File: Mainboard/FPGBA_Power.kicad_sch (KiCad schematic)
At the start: 21 parts, among them U1 LM3880, U3 TPS22917DBV, U4 TLV62569DBV, U5 TLV75533PDBV, U6 TLV75518PDBV

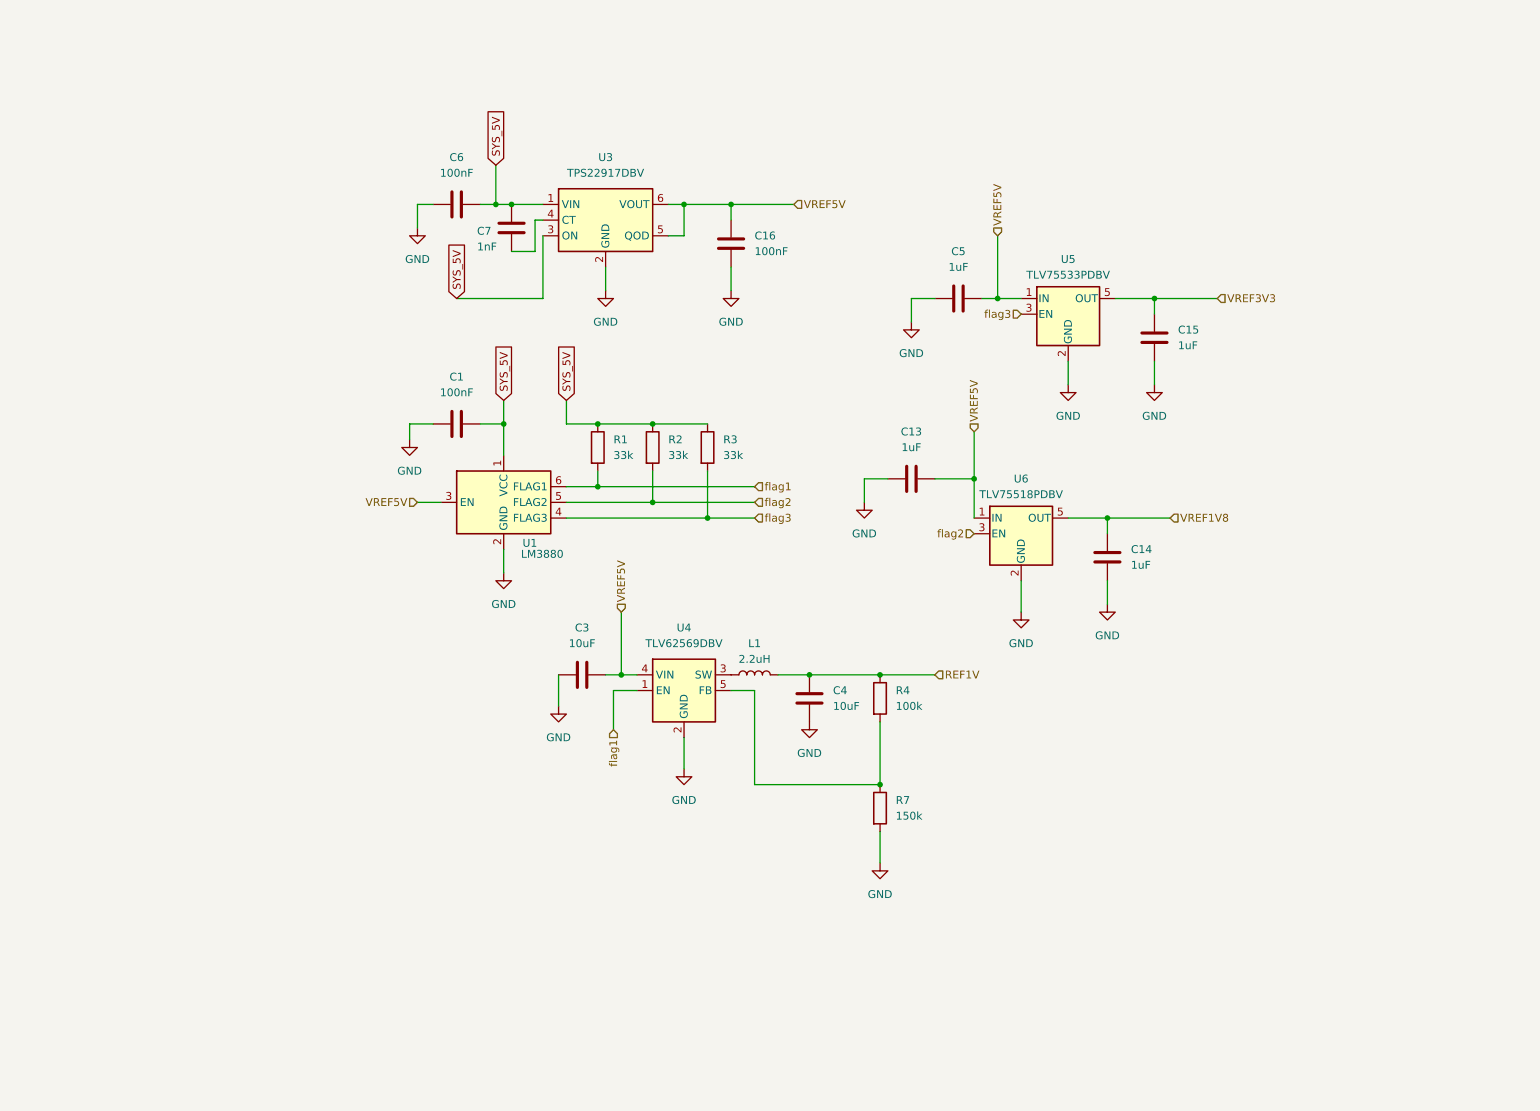
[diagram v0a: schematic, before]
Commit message: fixed heirarchy and dir structure
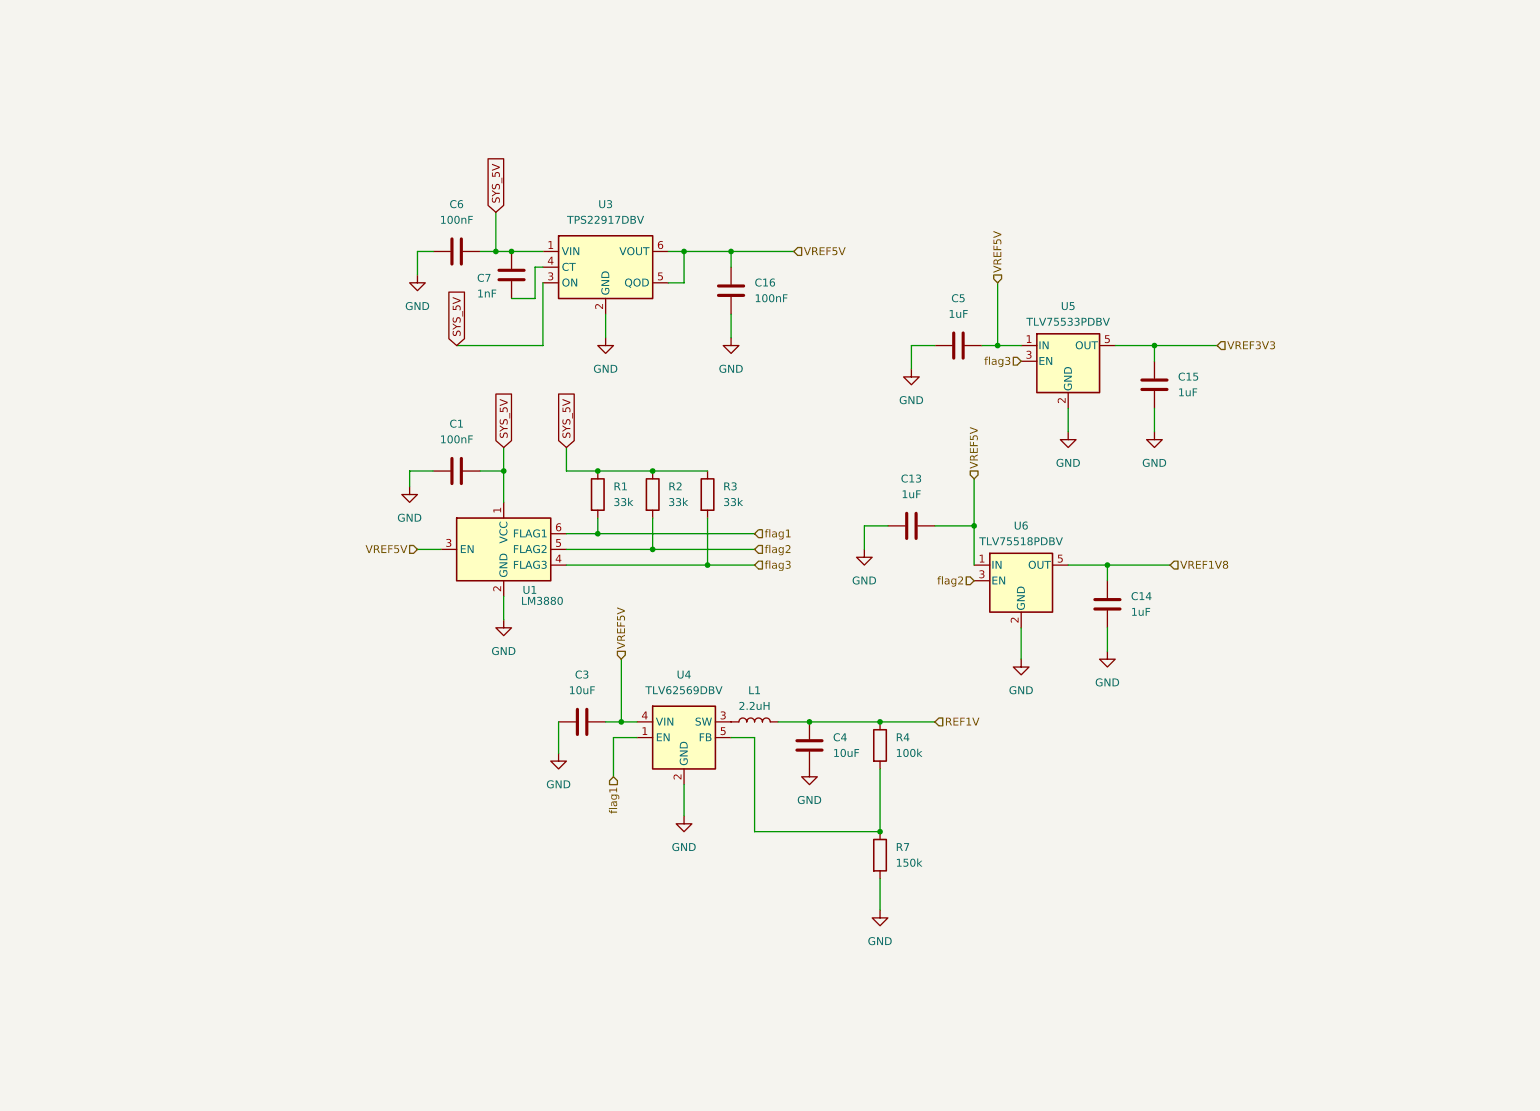
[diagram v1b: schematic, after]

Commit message: huge update: power/charging, audio, zif connections, screen, cartridge pinout
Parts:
- removed C15, C5: 1uF, Resistor_SMD:R_0603_1608Metric, symbol Device:C
- removed U5: TLV75533PDBV, Package_TO_SOT_SMD:SOT-23-5, symbol Regulator_Linear:TLV75533PDBV
- added C17: 10uF, Capacitor_SMD:C_0603_1608Metric, symbol Device:C
- added C18: 22uF, Capacitor_SMD:C_0603_1608Metric, symbol Device:C
- added IC3: XC7S50-L1CSGA324I, Package_BGA:BGA-324_15x15mm_Layout18x18_P0.8mm, symbol XC7S50-L1CSGA324I:XC7S50-L1CSGA324I
- added L3: 2.2uH, FPGBA:1206 (metric 2832), symbol Device:L
- added R10: 100k, Resistor_SMD:R_0603_1608Metric, symbol Device:R
- added R9: 453k, Resistor_SMD:R_0603_1608Metric, symbol Device:R
- added U7: TPS62822DLC, Package_SON:Texas_VSON-HR-8_1.5x2mm_P0.5mm, symbol Regulator_Switching:TPS62822DLC
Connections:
- net GND: now also C17.1, C18.1, IC3.A1 (GND_1), IC3.A12 (GND_2), IC3.A18 (GND_3), IC3.B9 (GND_4), IC3.C16 (GND_6), IC3.C6 (GND_5), IC3.D13 (GND_8), IC3.D3 (GND_7), IC3.E10 (GND_10), IC3.E8 (GND_9), IC3.F11 (GND_13), IC3.F17 (GND_14), IC3.F7 (GND_11), IC3.F9 (GND_12), IC3.G10 (GND_17), IC3.G12 (GND_18), IC3.G14 (GND_19), IC3.G4 (GND_15), IC3.G8 (GND_16), IC3.H1 (GND_20), IC3.H11 (GND_22), IC3.H7 (GND_21), IC3.J12 (GND_24), IC3.J18 (GND_25), IC3.J8 (GND_23), IC3.K15 (GND_29), IC3.K5 (GND_26), IC3.K7 (GND_27), IC3.L12 (GND_32), IC3.L2 (GND_30), IC3.L8 (GND_31), IC3.M11 (GND_35), IC3.M7 (GND_33), IC3.M9 (GND_34), IC3.N10 (GND_38), IC3.N12 (GND_39), IC3.N16 (GND_40), IC3.N6 (GND_36), IC3.N8 (GND_37), IC3.P11 (GND_43), IC3.P3 (GND_41), IC3.P9 (GND_42), IC3.R10 (GND_44), IC3.T17 (GND_46), IC3.T7 (GND_45), IC3.U14 (GND_48), IC3.U4 (GND_47), IC3.V1 (GND_49), IC3.V11 (GND_50), IC3.V18 (GND_51), R10.2, U7.3 (AGND), U7.5 (PGND)
- net REF1V: now also IC3.E11 (VCCINT_3), IC3.E7 (VCCINT_1), IC3.E9 (VCCINT_2), IC3.F10 (VCCINT_5), IC3.F8 (VCCINT_4), IC3.G11 (VCCINT_8), IC3.G7 (VCCINT_6), IC3.G9 (VCCINT_7), IC3.H8 (VCCINT_9), IC3.J11 (VCCINT_11), IC3.J7 (VCCINT_10), IC3.K8 (VCCINT_12), IC3.L11 (VCCINT_13), IC3.L7 (VCCBRAM_1), IC3.M10 (VCCINT_15), IC3.M8 (VCCINT_14), IC3.N11 (VCCINT_17), IC3.N7 (VCCBRAM_2), IC3.N9 (VCCINT_16), IC3.P10 (VCCINT_19), IC3.P8 (VCCINT_18)
- net SYS_5V: now also C17.2, U7.7 (VIN)
- net VREF1V8: now also IC3.F12 (VCCAUX_1), IC3.H12 (VCCAUX_2), IC3.M12 (VCCAUX_4), IC3.P12 (VCCAUX_5)
- net VREF3V3: now also C18.2, L3.2, R9.1
- net flag3: now also U7.1 (EN)
- new net: R10.1, R9.2, U7.2 (FB)
- new net: L3.1, U7.6 (SW)
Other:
- moved on the sheet: C1, C13, C14, C16, C3, C4, C6, C7, L1, R1, R2, R3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

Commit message: FPGA schematic and board images
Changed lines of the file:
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@@
+		)
+	)
+	(global_label "REF1V"
+		(shape input)
+		(at 187.96 123.19 180)
+		(fields_autoplaced yes)
+		(effects
+			(font
+				(size 1.27 1.27)
+			)
+			(justify right)
+		)
+		(property "Intersheetrefs" "${INTERSHEET_REFS}"
+			(at 179.1691 123.19 0)
+			(hide yes)
+			(show_name no)
+			(do_not_autoplace no)
+			(effects
+				(font
+					(size 1.27 1.27)
+				)
+				(justify right)
+			)
+		)
+	)
+	(global_label "REF1V"
+		(shape input)
+		(at 251.46 49.53 0)
+		(fields_autoplaced yes)
+		(effects
+			(font
+				(size 1.27 1.27)
+			)
+			(justify left)
+		)
+		(property "Intersheetrefs" "${INTERSHEET_REFS}"
+			(at 260.2509 49.53 0)
+			(hide yes)
+			(show_name no)
+			(do_not_autoplace no)
+			(effects
+				(font
+					(size 1.27 1.27)
+				)
+				(justify left)
+			)
+		)
+	)
+	(global_label "REF1V"
+		(shape input)
+		(at 187.96 135.89 180)
+		(fields_autoplaced yes)
+		(effects
+			(font
+				(size 1.27 1.27)
+			)
+			(justify right)
+		)
+		(property "Intersheetrefs" "${INTERSHEET_REFS}"
+			(at 179.1691 135.89 0)
+			(hide yes)
+			(show_name no)
+			(do_not_autoplace no)
+			(effects
+				(font
+					(size 1.27 1.27)
+				)
+				(justify right)
+			)
 		)
 	)
@@
 		)
 	)
+	(global_label "REF1V"
+		(shape input)
+		(at 251.46 77.47 0)
+		(fields_autoplaced yes)
+		(effects
+			(font
+				(size 1.27 1.27)
+			)
+			(justify left)
+		)
+		(property "Intersheetrefs" "${INTERSHEET_REFS}"
+			(at 260.2509 77.47 0)
+			(hide yes)
+			(show_name no)
+			(do_not_autoplace no)
+			(effects
+				(font
+					(size 1.27 1.27)
+				)
+				(justify left)
+			)
+		)
+	)
+	(global_label "REF1V"
+		(shape input)
+		(at 170.18 110.49 180)
+		(fields_autoplaced yes)
+		(effects
+			(font
+				(size 1.27 1.27)
+			)
+			(justify right)
+		)
+		(property "Intersheetrefs" "${INTERSHEET_REFS}"
+			(at 161.3891 110.49 0)
+			(hide yes)
+			(show_name no)
+			(do_not_autoplace no)
+			(effects
+				(font
+					(size 1.27 1.27)
+				)
+				(justify right)
+			)
+		)
+	)
+	(global_label "REF1V"
+		(shape input)
+		(at 170.18 82.55 180)
+		(fields_autoplaced yes)
+		(effects
+			(font
+				(size 1.27 1.27)
+			)
+			(justify right)
+		)
+		(property "Intersheetrefs" "${INTERSHEET_REFS}"
+			(at 161.3891 82.55 0)
+			(hide yes)
+			(show_name no)
+			(do_not_autoplace no)
+			(effects
+				(font
+					(size 1.27 1.27)
+				)
+				(justify right)
+			)
+		)
+	)
+	(global_label "REF1V"
+		(shape input)
+		(at 187.96 146.05 180)
+		(fields_autoplaced yes)
+		(effects
+			(font
+				(size 1.27 1.27)
+			)
+			(justify right)
+		)
+		(property "Intersheetrefs" "${INTERSHEET_REFS}"
+			(at 179.1691 146.05 0)
+			(hide yes)
+			(show_name no)
+			(do_not_autoplace no)
+			(effects
+				(font
+					(size 1.27 1.27)
+				)
+				(justify right)
+			)
+		)
+	)
 	(global_label "SYS_5V"
 		(shape input)
@@
 		)
 	)
+	(global_label "REF1V"
+		(shape input)
+		(at 109.22 109.22 0)
+		(fields_autoplaced yes)
+		(effects
+			(font
+				(size 1.27 1.27)
+			)
+			(justify left)
+		)
+		(property "Intersheetrefs" "${INTERSHEET_REFS}"
+			(at 118.0109 109.22 0)
+			(hide yes)
+			(show_name no)
+			(do_not_autoplace no)
+			(effects
+				(font
+					(size 1.27 1.27)
+				)
+				(justify left)
+			)
+		)
+	)
 	(global_label "SYS_5V"
 		(shape input)
@@
 		)
 	)
+	(global_label "REF1V"
+		(shape input)
+		(at 251.46 107.95 0)
+		(fields_autoplaced yes)
+		(effects
+			(font
+				(size 1.27 1.27)
+			)
+			(justify left)
+		)
+		(property "Intersheetrefs" "${INTERSHEET_REFS}"
+			(at 260.2509 107.95 0)
+			(hide yes)
+			(show_name no)
+			(do_not_autoplace no)
+			(effects
+				(font
+					(size 1.27 1.27)
+				)
+				(justify left)
+			)
+		)
+	)
 	(global_label "SYS_5V"
 		(shape input)
@@
 		)
 	)
+	(hierarchical_label "VREF1V8"
+		(shape input)
+		(at 147.32 83.82 0)
+		(effects
+			(font
+				(size 1.27 1.27)
+			)
+			(justify left)
+		)
+	)
+	(hierarchical_label "flag3"
+		(shape input)
+		(at 80.01 83.82 0)
+		(effects
+			(font
+				(size 1.27 1.27)
+			)
+			(justify left)
+		)
+	)
+	(hierarchical_label "VREF5V"
+		(shape input)
+		(at 25.4 81.28 180)
+		(effects
+			(font
+				(size 1.27 1.27)
+			)
+			(justify right)
+		)
+	)
+	(hierarchical_label "VREF1V8"
+		(shape input)
+		(at 233.68 113.03 0)
+		(effects
+			(font
+				(size 1.27 1.27)
+			)
+			(justify left)
+		)
+	)
 	(hierarchical_label "REF1V"
 		(shape input)
-		(at 170.18 110.49 180)
-		(effects
-			(font
-				(size 1.27 1.27)
-			)
-			(justify right)
-		)
-	)
-	(hierarchical_label "VREF1V8"
-		(shape input)
-		(at 147.32 83.82 0)
-		(effects
-			(font
-				(size 1.27 1.27)
-			)
-			(justify left)
-		)
-	)
-	(hierarchical_label "flag3"
-		(shape input)
-		(at 80.01 83.82 0)
-		(effects
-			(font
-				(size 1.27 1.27)
-			)
-			(justify left)
-		)
-	)
-	(hierarchical_label "REF1V"
-		(shape input)
-		(at 251.46 49.53 0)
-		(effects
-			(font
-				(size 1.27 1.27)
-			)
-			(justify left)
-		)
-	)
-	(hierarchical_label "REF1V"
-		(shape input)
-		(at 109.22 109.22 0)
-		(effects
-			(font
-				(size 1.27 1.27)
-			)
-			(justify left)
-		)
-	)
-	(hierarchical_label "REF1V"
-		(shape input)
-		(at 187.96 123.19 180)
-		(effects
-			(font
-				(size 1.27 1.27)
-			)
-			(justify right)
-		)
-	)
-	(hierarchical_label "REF1V"
-		(shape input)
-		(at 187.96 135.89 180)
-		(effects
-			(font
-				(size 1.27 1.27)
-			)
-			(justify right)
-		)
-	)
-	(hierarchical_label "REF1V"
-		(shape input)
-		(at 251.46 107.95 0)
-		(effects
-			(font
-				(size 1.27 1.27)
-			)
-			(justify left)
-		)
-	)
-	(hierarchical_label "REF1V"
-		(shape input)
-		(at 251.46 77.47 0)
+		(at 233.68 29.21 0)
 		(effects
 			(font
@@
 	(hierarchical_label "VREF5V"
 		(shape input)
-		(at 25.4 81.28 180)
-		(effects
-			(font
-				(size 1.27 1.27)
-			)
-			(justify right)
-		)
-	)
-	(hierarchical_label "VREF1V8"
-		(shape input)
-		(at 233.68 113.03 0)
-		(effects
-			(font
-				(size 1.27 1.27)
-			)
-			(justify left)
-		)
-	)
-	(hierarchical_label "REF1V"
-		(shape input)
-		(at 233.68 29.21 0)
-		(effects
-			(font
-				(size 1.27 1.27)
-			)
-			(justify left)
-		)
-	)
-	(hierarchical_label "REF1V"
-		(shape input)
-		(at 187.96 146.05 180)
-		(effects
-			(font
-				(size 1.27 1.27)
-			)
-			(justify right)
-		)
-	)
-	(hierarchical_label "VREF5V"
-		(shape input)
 		(at 86.36 33.02 0)
 		(effects
@@
 		)
 	)
-	(hierarchical_label "REF1V"
-		(shape input)
-		(at 170.18 82.55 180)
-		(effects
-			(font
-				(size 1.27 1.27)
-			)
-			(justify right)
-		)
-	)
